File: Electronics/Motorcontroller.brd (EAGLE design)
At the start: 101.3 x 50.8 mm, 45 parts, among them Q1 IRFZ48V, Q2 IRF4905V, Q3 IRFZ48V, Q4 IRF4905V, Q5 IRFZ48V, Q6 IRF4905V, Q7 IRFZ48V, Q8 IRF4905V, T1 BC547, T2 BC547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

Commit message: Added LEDs to optocoupelers. Closes #39
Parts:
- added LED10, LED11, LED6, LED7, LED8, LED9: (no value), led:LED3MM
- R14, R19: value 330 -> 150
- R15, R16, R17, R18: value 330 -> 150; device rcl:0207/7 -> rcl:0207/5V
- moved R14 5.72 mm to (14.3, 40.6)
- moved R19 2.93 mm to (81.3, 37.5)
- moved R15 2.29 mm to (30.8, 38.1)
- moved R16 2.01 mm to (43.5, 38.7)
- moved R17 2.01 mm to (56.2, 38.7)
- moved R18 2.01 mm to (68.9, 38.7)
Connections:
- removed net N$36: OK5.1, R18.2
- removed net N$37: OK6.1, R19.2
- new net N$17: LED10.A, R18.2
- new net N$20: LED6.A, R14.2
- new net N$26: LED7.A, R15.2
- new net N$27: LED8.A, R16.2
- new net N$28: LED9.A, R17.2
- new net N$33: LED9.K, OK4.1
- new net N$34: LED10.K, OK5.1
- new net N$35: LED11.K, OK6.1
- net N$29: now also LED11.A, R19.2; no longer OK1.1, R14.2
- net N$30: now also LED6.K, OK1.1; no longer OK2.1, R15.2
- net N$31: now also LED7.K, OK2.1; no longer OK3.1, R16.2
- net N$32: now also LED8.K, OK3.1; no longer OK4.1, R17.2
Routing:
- net N$3: track 9.84 -> 4.13 mm
- net N$35: track 0.00 -> 4.23 mm, vias 1 -> 0
- net N$33: track 0.00 -> 4.23 mm, vias 1 -> 0
- net N$34: track 0.00 -> 4.23 mm, vias 1 -> 0
- net N$26: track 0.00 -> 3.94 mm, vias 1 -> 0
- net N$37: track 3.65 -> 0.00 mm
- net N$36: track 3.65 -> 0.00 mm
- net N$20: track 0.00 -> 3.49 mm, vias 1 -> 0
- net N$27: track 0.00 -> 3.31 mm, vias 1 -> 0
- net N$28: track 0.00 -> 3.31 mm, vias 1 -> 0
- net N$17: track 0.00 -> 3.31 mm, vias 1 -> 0
- net N$11: track 89.2 -> 86.2 mm
- net GND: track 97.1 -> 99.3 mm
- net N$10: track 63.3 -> 61.1 mm
- net N$5: track 26.0 -> 24.1 mm
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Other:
- board text added: "Motorcontroller v5.1"
- board text removed: "Motorcontroller v5.0"

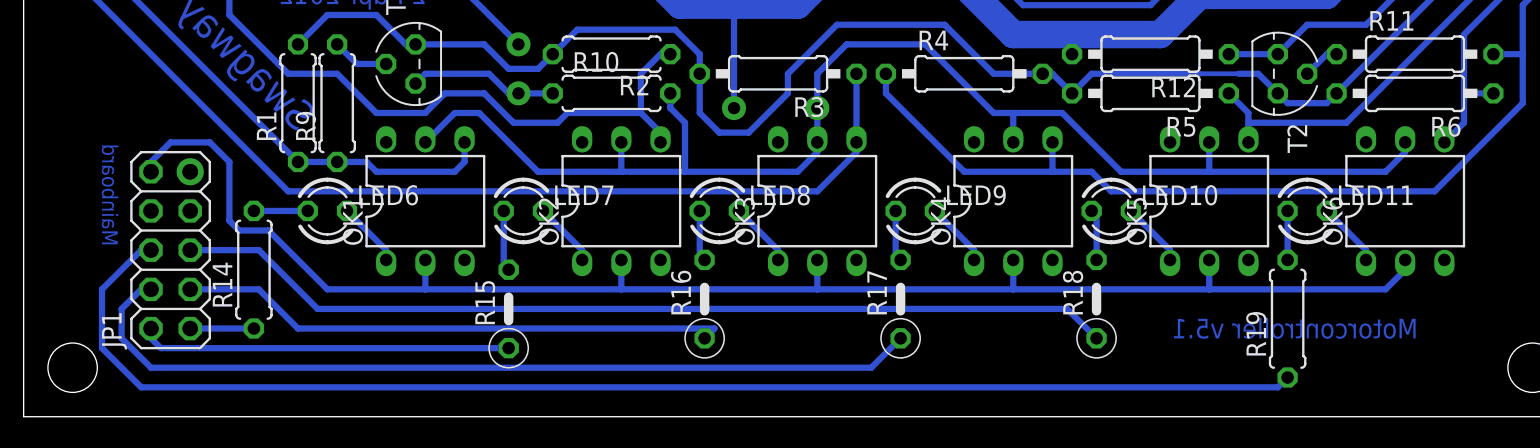
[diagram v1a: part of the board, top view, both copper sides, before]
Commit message: Changed pins on pinheader
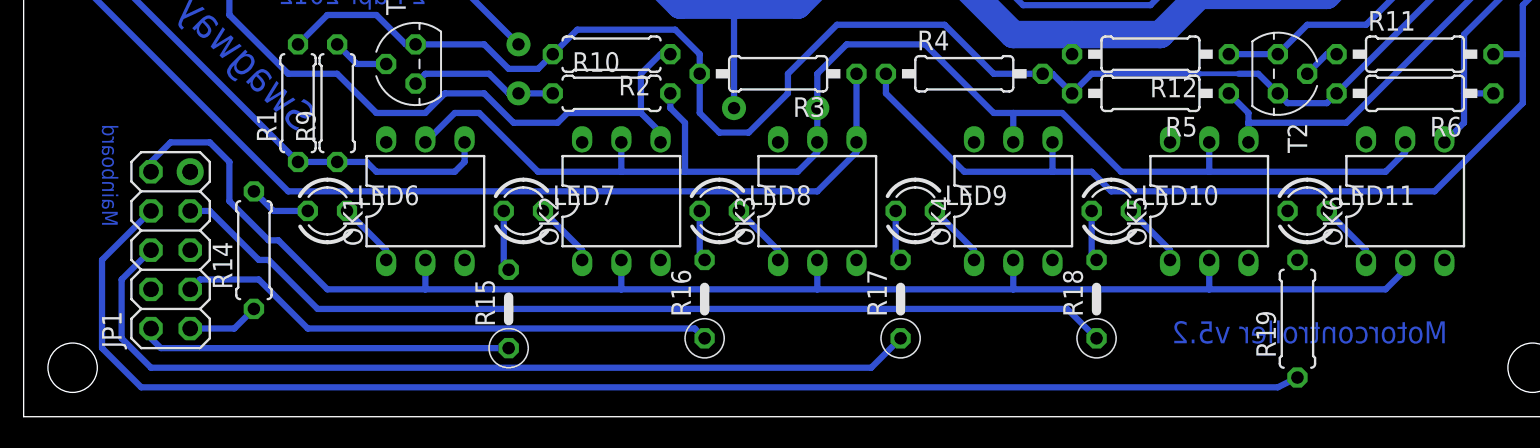
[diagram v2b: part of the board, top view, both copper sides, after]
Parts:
- moved R14 1.27 mm to (14.3, 41.9)
- moved R19 0.64 mm to (81.9, 37.5)
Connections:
- net N$10: now also JP1.7; no longer JP1.5
- net N$11: now also JP1.8; no longer JP1.6
- net N$8: now also JP1.6; no longer JP1.4
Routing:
- net N$29: track 3.18 -> 0.00 mm
- net N$11: track 86.2 -> 88.9 mm
- net N$8: track 56.4 -> 58.6 mm
- net N$10: track 61.1 -> 62.2 mm
- net GND: track 99.3 -> 98.6 mm
- net N$7: track 35.9 -> 35.2 mm
- net N$3: track 4.13 -> 4.65 mm
- net N$20: track 3.49 -> 4.02 mm
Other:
- board text added: "Motorcontroller v5.2"
- board text removed: "Motorcontroller v5.1"
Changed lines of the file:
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@@
 <setting verticaltext="up"/>
 </settings>
-<grid distance="0.0125" unitdist="inch" unit="inch" style="dots" multiple="4" display="yes" altdistance="0.025" altunitdist="inch" altunit="inch"/>
+<grid distance="0.025" unitdist="inch" unit="inch" style="dots" multiple="4" display="yes" altdistance="0.025" altunitdist="inch" altunit="inch"/>
 <layers>
 <layer number="1" name="Top" color="4" fill="1" visible="no" active="yes"/>
@@
 <hole x="97.155" y="34.29" drill="3.2"/>
 <text x="57.531" y="71.755" size="2.54" layer="16" rot="MR0">+</text>
-<text x="89.7300125" y="36.190484375" size="1.27" layer="16" rot="MR0">Motorcontroller v5.1</text>
-<text x="4.445" y="42.164" size="1.016" layer="16" rot="MR90">Mainboard</text>
+<text x="91.6350125" y="35.872984375" size="1.4224" layer="16" rot="MR0">Motorcontroller v5.2</text>
+<text x="4.445" y="43.434" size="1.016" layer="16" rot="MR90">Mainboard</text>
 <text x="25.458984375" y="57.853009375" size="1.27" layer="16" rot="MR0">24 apr 2012</text>
 <text x="69.215" y="78.74" size="1.016" layer="16" rot="MR0">Carl-Emil Grøn Christensen</text>
@@
 <element name="T2" library="transistor" package="TO92" value="BC547" x="80.645" y="53.34" rot="R270"/>
 <element name="R12" library="rcl" package="0207/10" value="10k" x="72.39" y="54.61" rot="R180"/>
-<element name="R14" library="rcl" package="0207/7" value="150" x="14.2875" y="40.64" rot="R90"/>
+<element name="R14" library="rcl" package="0207/7" value="150" x="14.2875" y="41.91" rot="R90"/>
 <element name="R15" library="rcl" package="0207/5V" value="150" x="30.7975" y="38.1" rot="R90"/>
 <element name="R16" library="rcl" package="0207/5V" value="150" x="43.4975" y="38.735" rot="R90"/>
 <element name="R17" library="rcl" package="0207/5V" value="150" x="56.1975" y="38.735" rot="R90"/>
 <element name="R18" library="rcl" package="0207/5V" value="150" x="68.8975" y="38.735" rot="R90"/>
-<element name="R19" library="rcl" package="0207/7" value="150" x="81.28" y="37.465" rot="R90"/>
+<element name="R19" library="rcl" package="0207/7" value="150" x="81.915" y="37.465" rot="R90"/>
 <element name="LED6" library="led" package="LED3MM" value="" x="19.05" y="44.45"/>
 <element name="LED7" library="led" package="LED3MM" value="" x="31.75" y="44.45"/>
@@
 <wire x1="7.62" y1="47.625" x2="7.62" y2="46.99" width="0.4064" layer="16"/>
 <wire x1="11.43" y1="48.895" x2="12.7" y2="47.625" width="0.4064" layer="16"/>
-<wire x1="12.7" y1="47.625" x2="12.7" y2="43.815" width="0.4064" layer="16"/>
-<wire x1="12.7" y1="43.815" x2="13.335" y2="43.18" width="0.4064" layer="16"/>
-<wire x1="13.335" y1="43.18" x2="15.24" y2="43.18" width="0.4064" layer="16"/>
-<wire x1="15.24" y1="43.18" x2="19.05" y2="39.37" width="0.4064" layer="16"/>
 <wire x1="19.05" y1="39.37" x2="25.4" y2="39.37" width="0.4064" layer="16"/>
+<wire x1="15.24" y1="42.545" x2="12.7" y2="45.085" width="0.4064" layer="16"/>
+<wire x1="12.7" y1="45.085" x2="12.7" y2="47.625" width="0.4064" layer="16"/>
+<wire x1="15.24" y1="42.545" x2="15.875" y2="42.545" width="0.4064" layer="16"/>
+<wire x1="15.875" y1="42.545" x2="19.05" y2="39.37" width="0.4064" layer="16"/>
 </signal>
 <signal name="N$2">
@@
 <contactref element="JP1" pad="1"/>
 <contactref element="R14" pad="1"/>
-<wire x1="14.2875" y1="36.83" x2="10.16" y2="36.83" width="0.4064" layer="16"/>
+<wire x1="10.16" y1="36.83" x2="13.0175" y2="36.83" width="0.4064" layer="16"/>
+<wire x1="13.0175" y1="36.83" x2="14.2875" y2="38.1" width="0.4064" layer="16"/>
 </signal>
 <signal name="N$7">
 <contactref element="JP1" pad="3"/>
 <contactref element="R16" pad="1"/>
-<wire x1="44.1325" y1="36.83" x2="17.145" y2="36.83" width="0.4064" layer="16"/>
-<wire x1="44.1325" y1="36.83" x2="43.4975" y2="36.195" width="0.4064" layer="16"/>
-<wire x1="10.16" y1="39.37" x2="14.605" y2="39.37" width="0.4064" layer="16"/>
-<wire x1="14.605" y1="39.37" x2="17.145" y2="36.83" width="0.4064" layer="16"/>
+<wire x1="10.16" y1="39.37" x2="10.795" y2="40.005" width="0.4064" layer="16"/>
+<wire x1="10.795" y1="40.005" x2="14.605" y2="40.005" width="0.4064" layer="16"/>
+<wire x1="14.605" y1="40.005" x2="17.78" y2="36.83" width="0.4064" layer="16"/>
+<wire x1="17.78" y1="36.83" x2="42.8625" y2="36.83" width="0.4064" layer="16"/>
+<wire x1="42.8625" y1="36.83" x2="43.4975" y2="36.195" width="0.4064" layer="16"/>
 </signal>
 <signal name="N$8">
-<contactref element="JP1" pad="4"/>
 <contactref element="R17" pad="1"/>
-<wire x1="5.715" y1="38.1" x2="5.715" y2="36.195" width="0.4064" layer="16"/>
 <wire x1="5.715" y1="36.195" x2="7.62" y2="34.29" width="0.4064" layer="16"/>
-<wire x1="7.62" y1="39.37" x2="6.985" y2="39.37" width="0.4064" layer="16"/>
-<wire x1="6.985" y1="39.37" x2="5.715" y2="38.1" width="0.4064" layer="16"/>
 <wire x1="7.62" y1="34.29" x2="54.2925" y2="34.29" width="0.4064" layer="16"/>
 <wire x1="54.2925" y1="34.29" x2="56.1975" y2="36.195" width="0.4064" layer="16"/>
+<contactref element="JP1" pad="6"/>
+<wire x1="5.715" y1="36.195" x2="5.715" y2="40.005" width="0.4064" layer="16"/>
+<wire x1="5.715" y1="40.005" x2="7.62" y2="41.91" width="0.4064" layer="16"/>
 </signal>
 <signal name="N$10">
-<contactref element="JP1" pad="5"/>
 <contactref element="R18" pad="1"/>
-<wire x1="18.415" y1="38.1" x2="14.605" y2="41.91" width="0.4064" layer="16"/>
-<wire x1="14.605" y1="41.91" x2="10.16" y2="41.91" width="0.4064" layer="16"/>
 <wire x1="18.415" y1="38.1" x2="66.9925" y2="38.1" width="0.4064" layer="16"/>
 <wire x1="66.9925" y1="38.1" x2="68.8975" y2="36.195" width="0.4064" layer="16"/>
+<contactref element="JP1" pad="7"/>
+<wire x1="10.16" y1="44.45" x2="11.43" y2="44.45" width="0.4064" layer="16"/>
+<wire x1="11.43" y1="44.45" x2="14.605" y2="41.275" width="0.4064" layer="16"/>
+<wire x1="14.605" y1="41.275" x2="15.24" y2="41.275" width="0.4064" layer="16"/>
+<wire x1="15.24" y1="41.275" x2="18.415" y2="38.1" width="0.4064" layer="16"/>
 </signal>
 <signal name="N$11">
-<contactref element="JP1" pad="6"/>
 <contactref element="R19" pad="1"/>
-<wire x1="4.445" y1="39.37" x2="4.445" y2="35.56" width="0.4064" layer="16"/>
+<wire x1="4.445" y1="41.275" x2="4.445" y2="35.56" width="0.4064" layer="16"/>
 <wire x1="4.445" y1="35.56" x2="6.985" y2="33.02" width="0.4064" layer="16"/>
-<wire x1="7.62" y1="41.91" x2="6.985" y2="41.91" width="0.4064" layer="16"/>
-<wire x1="6.985" y1="41.91" x2="4.445" y2="39.37" width="0.4064" layer="16"/>
 <wire x1="6.985" y1="33.02" x2="80.645" y2="33.02" width="0.4064" layer="16"/>
-<wire x1="80.645" y1="33.02" x2="81.28" y2="33.655" width="0.4064" layer="16"/>
+<wire x1="80.645" y1="33.02" x2="81.915" y2="33.655" width="0.4064" layer="16"/>
+<contactref element="JP1" pad="8"/>
+<wire x1="4.445" y1="41.275" x2="7.62" y2="44.45" width="0.4064" layer="16"/>
 </signal>
 <signal name="N$23">
@@
 <contactref element="R14" pad="2"/>
 <contactref element="LED6" pad="A"/>
-<wire x1="14.2875" y1="44.45" x2="17.78" y2="44.45" width="0.4064" layer="16"/>
+<wire x1="17.78" y1="44.45" x2="15.5575" y2="44.45" width="0.4064" layer="16"/>
+<wire x1="15.5575" y1="44.45" x2="14.2875" y2="45.72" width="0.4064" layer="16"/>
 </signal>
 <signal name="N$27">
@@
 <contactref element="R18" pad="2"/>
 <contactref element="LED10" pad="A"/>
-<wire x1="68.8975" y1="41.275" x2="68.8975" y2="44.1325" width="0.4064" layer="16"/>
-<wire x1="68.8975" y1="44.1325" x2="68.58" y2="44.45" width="0.4064" layer="16"/>
+<wire x1="68.58" y1="44.45" x2="68.58" y2="41.5925" width="0.4064" layer="16"/>
+<wire x1="68.58" y1="41.5925" x2="68.8975" y2="41.275" width="0.4064" layer="16"/>
 </signal>
 <signal name="N$29">
 <contactref element="R19" pad="2"/>
 <contactref element="LED11" pad="A"/>
-<wire x1="81.28" y1="44.45" x2="81.28" y2="41.275" width="0.4064" layer="16"/>
+<wire x1="81.28" y1="44.45" x2="81.915" y2="41.275" width="0" layer="19" extent="1-16"/>
 </signal>
 <signal name="N$30">

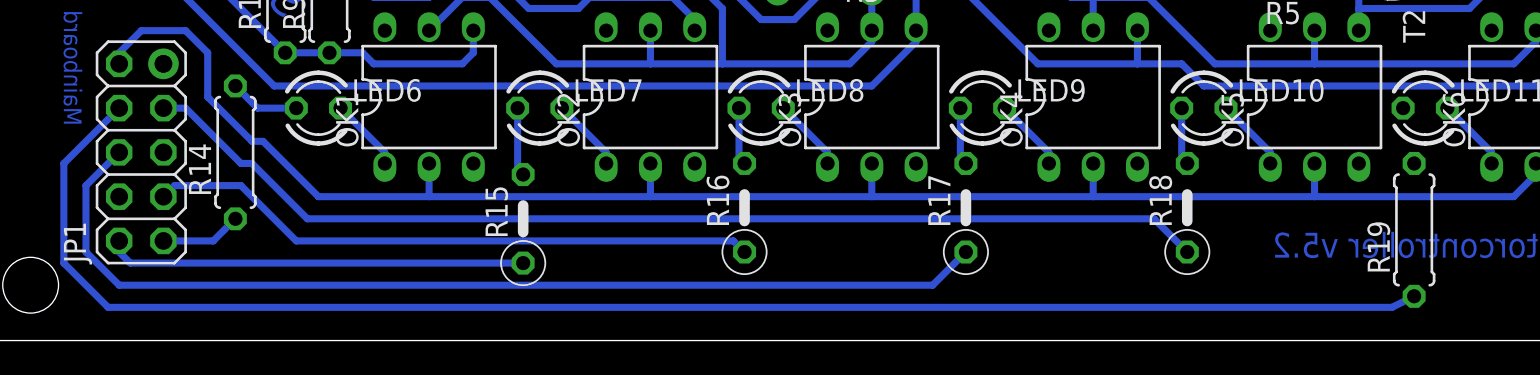
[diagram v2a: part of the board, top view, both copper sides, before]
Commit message: Route of small airwire
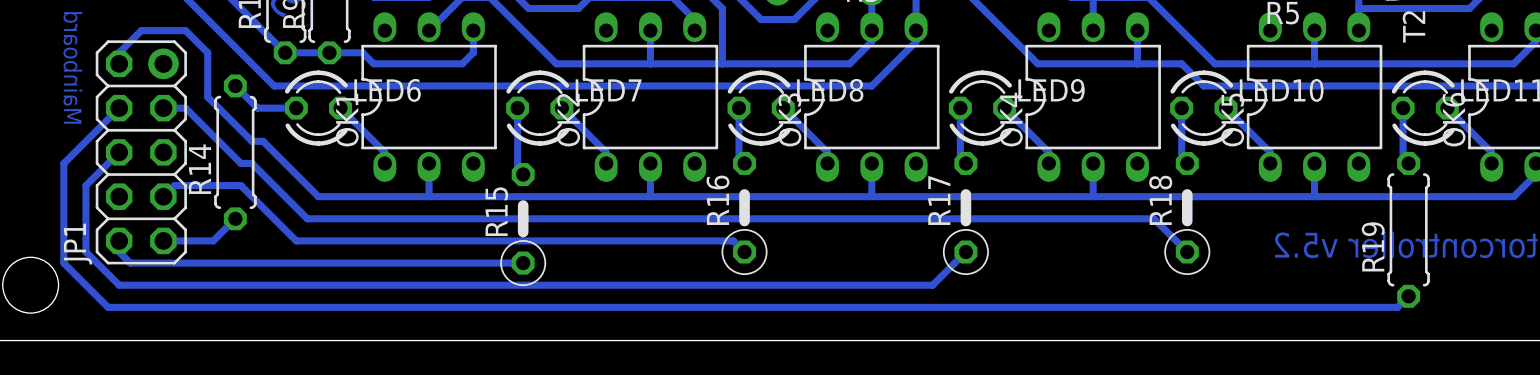
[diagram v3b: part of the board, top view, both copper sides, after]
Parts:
- moved R19 0.32 mm to (81.6, 37.5)
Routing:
- net N$29: track 0.00 -> 3.31 mm

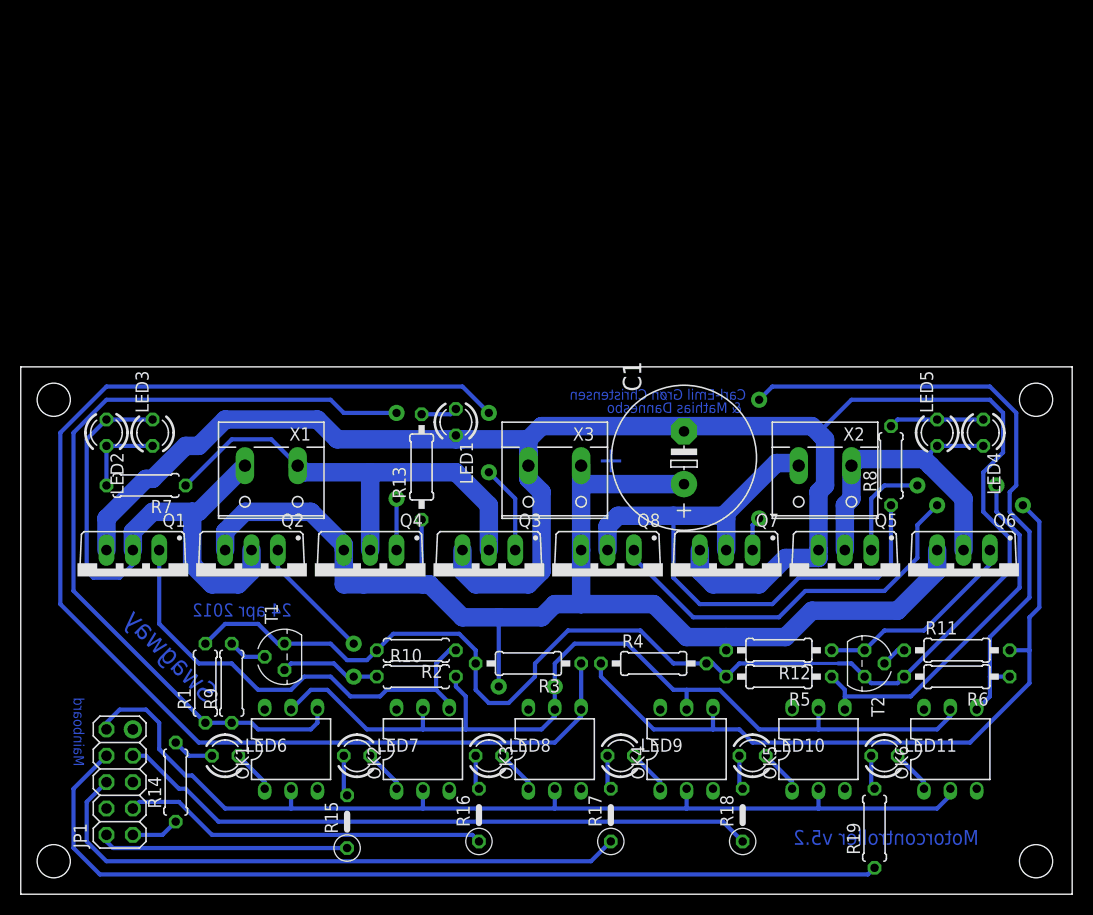
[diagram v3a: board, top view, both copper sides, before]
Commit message: Motorcontroller with protection diodes. Also closes #40
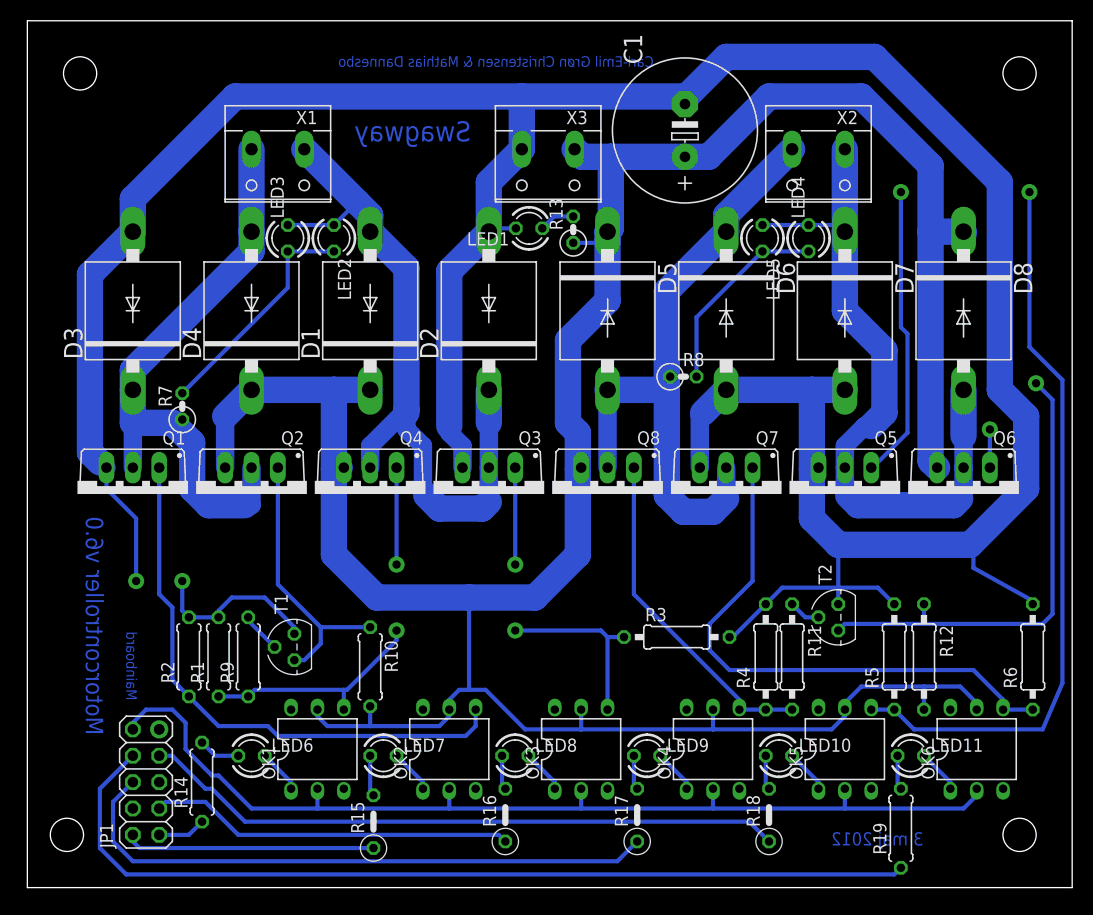
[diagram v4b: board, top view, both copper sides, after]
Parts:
- added D1, D2, D3, D4, D5, D6, D7, D8: P600, diode:P6-15
- R13: device rcl:0207/10 -> rcl:0207/2V
- R7, R8: device rcl:0207/7 -> rcl:0207/2V
- moved C1 31.5 mm to (63.3, 104.7)
- moved X1 30.5 mm to (24.1, 102.2)
- moved X2 30.5 mm to (76.2, 102.2)
- moved X3 30.5 mm to (50.2, 102.2)
- moved LED2 28.8 mm to (29.5, 94.3)
- moved R13 27.1 mm to (52.6, 95.1)
- moved LED4 25.2 mm to (75.2, 94.3), turned to 90 degrees
- moved LED5 25.2 mm to (70.8, 94.3), turned to 270 degrees
- moved LED3 22.8 mm to (25.1, 94.3)
- moved R2 21.9 mm to (15.6, 54.0), turned to 90 degrees
- moved R8 21.8 mm to (63.2, 81.0), turned to 0 degrees
- moved LED1 20.0 mm to (48.3, 95.2), turned to 180 degrees
- moved R11 15.9 mm to (73.7, 54.0), turned to 270 degrees
- moved R3 14.5 mm to (62.5, 55.9), turned to 0 degrees
- moved R12 14.0 mm to (86.4, 54.0), turned to 270 degrees
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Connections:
- removed net N$2: Q3.D, Q4.D, R7.1, X1.1
- removed net N$25: Q7.D, Q8.D, R8.1, X2.2
- new net N$36: D1.A, D2.C, LED2.A, LED3.K, Q3.D, Q4.D, X1.1
- new net N$43: D5.A, D6.C, Q7.D, Q8.D, R8.1, X2.2
- net +24V: now also D1.C, D4.C, D5.C, D8.C
- net GND2: now also D2.A, D3.A, D6.A, D7.A
- net N$1: now also D7.C, D8.A
- net N$4: now also D3.C, D4.A, R7.1; no longer LED2.A, LED3.K
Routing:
- net N$13: track 131.0 -> 27.1 mm
- net N$16: track 108.2 -> 32.6 mm, vias 2 -> 0
- net N$36: track 0.00 -> 70.4 mm
- net N$25: track 62.0 -> 0.00 mm
- net N$43: track 0.00 -> 61.4 mm
- net +24V: track 211.1 -> 269.6 mm, vias 2 -> 0
- net N$21: track 45.6 -> 99.1 mm
- net N$12: track 83.7 -> 31.6 mm, vias 2 -> 1
- net GND2: track 265.2 -> 315.2 mm
- net N$2: track 45.5 -> 0.00 mm, vias 0 -> 1
- net N$1: track 32.6 -> 66.7 mm
- net N$19: track 20.1 -> 49.8 mm, vias 0 -> 2
- net N$23: track 8.26 -> 22.3 mm
- net N$24: track 9.15 -> 19.1 mm
- net N$22: track 63.3 -> 53.3 mm, vias 2 -> 0
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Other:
- board size 101.3 x 50.8 mm -> 100.6 x 83.5 mm
- board text added: "3 maj 2012"
- board text added: "Carl-Emil Grøn Christensen & Mathias Dannesbo"
- board text added: "Motorcontroller v6.0"
- board text removed: "& Mathias Dannesbo"
- board text removed: "24 apr 2012"
- board text removed: "Carl-Emil Grøn Christensen"
- board text removed: "Motorcontroller v5.2"
